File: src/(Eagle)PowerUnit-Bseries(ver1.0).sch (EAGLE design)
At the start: 142 parts, among them CON1 XT90PW-M, CON2 XT90PW-F, CON3 XT60PW-F, CON4 XT60PW-F, CON5 XT60PW-F, CON6 XT60PW-F, Q2 SSM3J332R, Q4 SSM3J332R, SW1 SS-12SDP2, SW2 RDS-16S-1055-SMT-TR, U1 LQFP64, U2 MCP2517FD, U3 CH340E, U5 AP63205WU-7, U7 AP331AWG-7, U9 AP331AWG-7, X1 XRCGB40M000F4M00R0, X2 RH100-24.000-18-1020-EXT-TR, X3 32.768K12.5PI/MC306

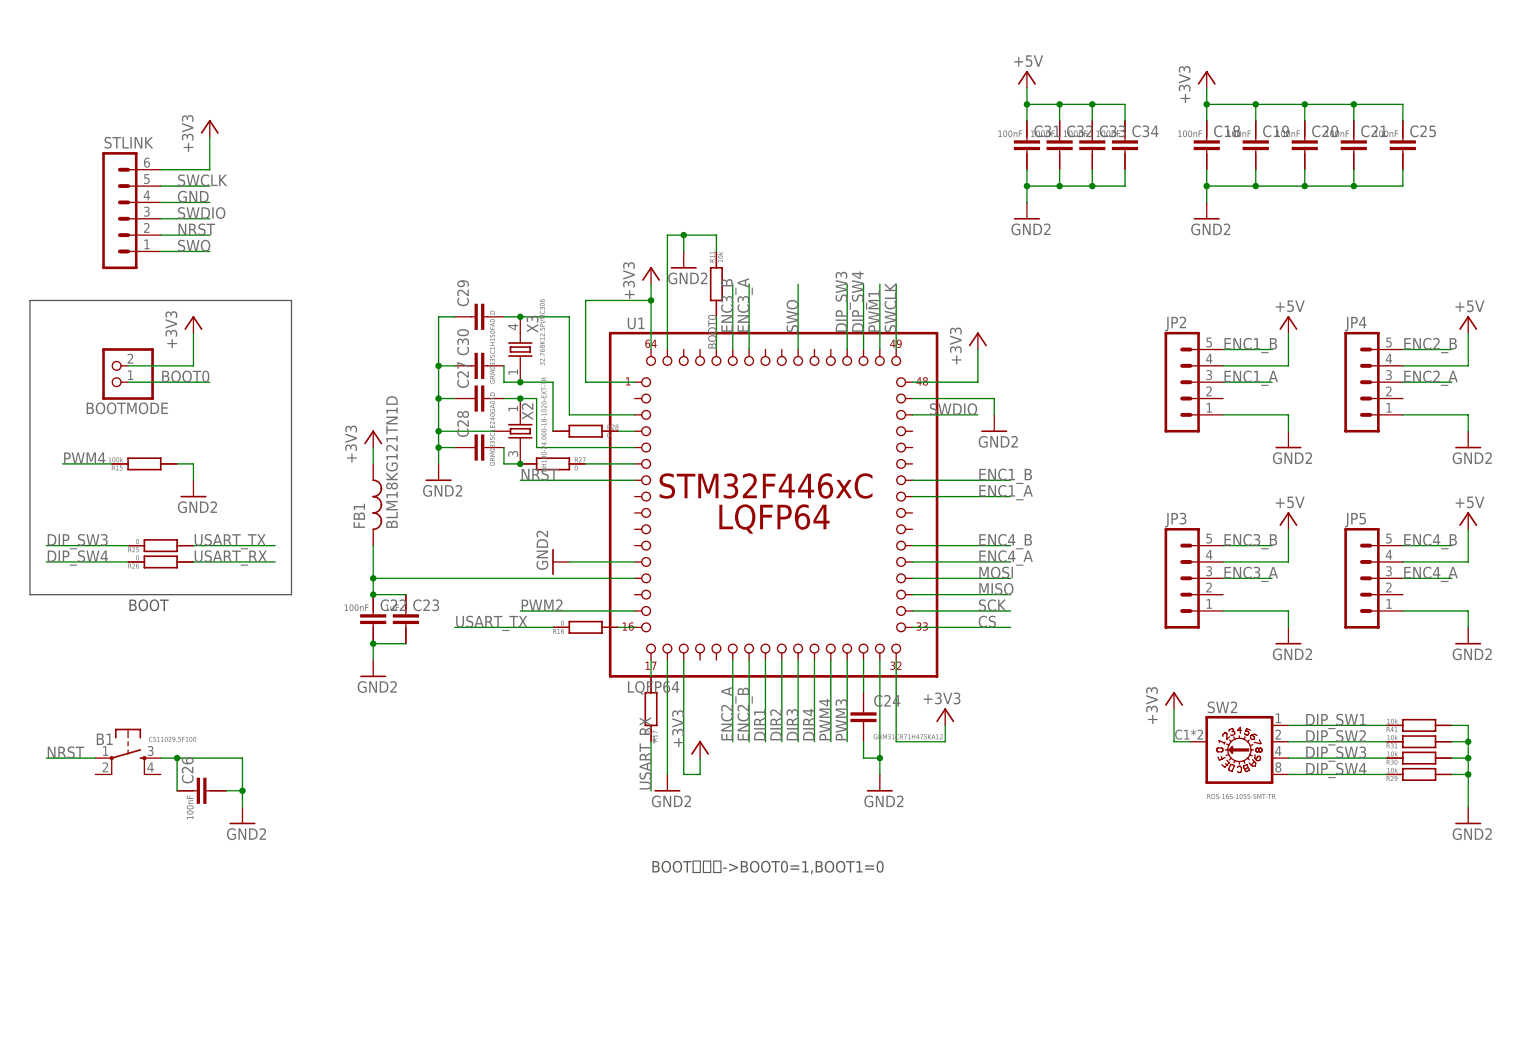
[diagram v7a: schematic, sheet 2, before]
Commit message: RJ45の追加
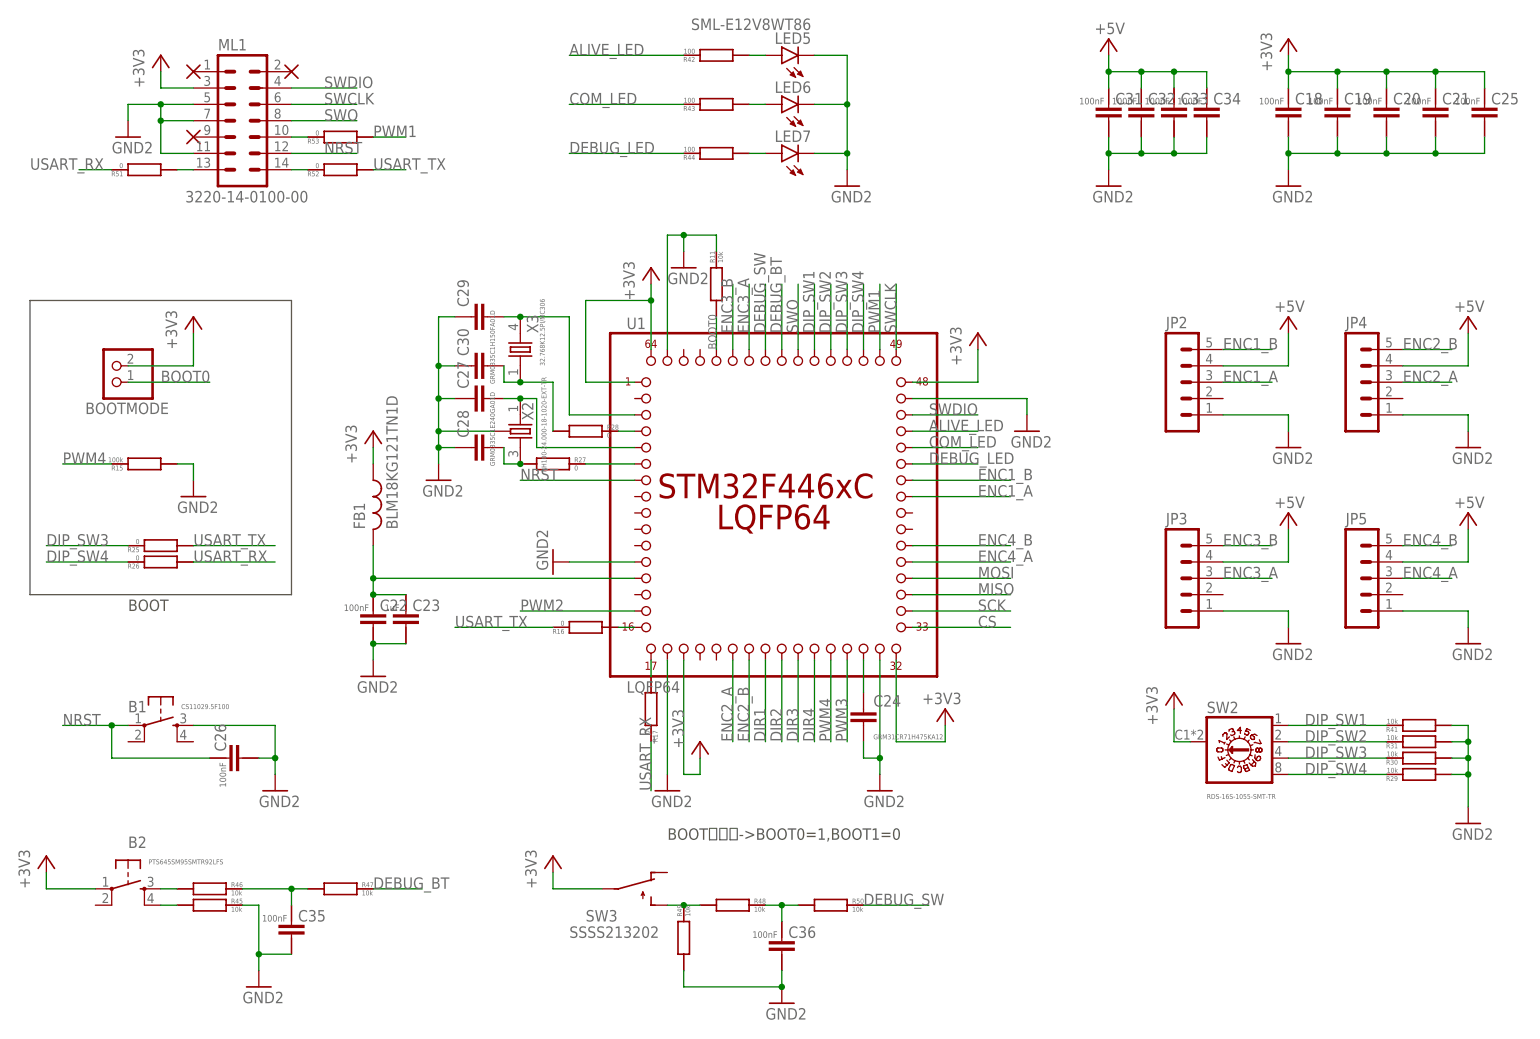
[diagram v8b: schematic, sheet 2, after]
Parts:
- removed STLINK: (no value), con-jst-xh:06-JST
- added B2: PTS645SM95SMTR92LFS, PTS645SM95SMTR92LFS:PTS645SM95SMTR92LFS
- added C35, C36: GCM188L81H104KA57, GCM188L81H104K57(0.1uF):GCM188L81H104KA57
- added LED5, LED6, LED7: SML-E12V8WT86, SML-E12V8WT86:SML-E12V8WT86
- added ML1: 3220-14-0100-00, 3220-14-0100-00:3220-14-0100-00
- added R42, R43, R44: 100, CR0603:CR0603
- added R45, R46, R47, R48, R49, R50: 10k, CR0603:CR0603
- added R51, R52, R53: 0, CR0603:CR0603
- added SW3: SSSS213202, SSSS213202:SSSS213202
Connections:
- new net ALIVE_LED: R42.RIGHT, U1.P45
- new net COM_LED: R43.RIGHT, U1.P44
- new net DEBUG_BT: C35.P$1, R46.RIGHT, R47.LEFT, R47.RIGHT, U1.P56
- new net DEBUG_LED: R44.RIGHT, U1.P43
- new net DEBUG_SW: R50.RIGHT, U1.P57
- new net N$58: LED5.A, R42.LEFT
- new net N$59: LED6.A, R43.LEFT
- new net N$60: LED7.A, R44.LEFT
- new net N$61: B2.4, R45.LEFT
- new net N$62: B2.3, R46.LEFT
- new net N$63: R48.LEFT, R49.RIGHT, SW3.R
- new net N$64: ML1.13, R51.LEFT
- new net N$65: C36.P$1, R48.RIGHT, R50.LEFT
- new net N$66: ML1.14, R52.RIGHT
- new net N$67: ML1.10, R53.RIGHT
- net +3V3: now also B2.1, ML1.3, SW3.C; no longer STLINK.6
- net DIP_SW1: now also U1.P54
- net DIP_SW2: now also U1.P53
- net GND: no longer STLINK.4
- net GND2: now also C35.P$2, C36.P$2, LED5.C, LED6.C, LED7.C, ML1.11, ML1.5, ML1.7, R45.RIGHT, R49.LEFT; no longer C26.P$1
- net NRST: now also C26.P$1, ML1.12; no longer STLINK.2
- net PWM1: now also R53.LEFT
- net SWCLK: now also ML1.6; no longer STLINK.5
- net SWDIO: now also ML1.4; no longer STLINK.3
- net SWO: now also ML1.8; no longer STLINK.1
- net USART_RX: now also R51.RIGHT
- net USART_TX: now also R52.LEFT
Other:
- moved on the sheet: B1, C18, C19, C20, C21, C25, C26, C31, C32, C33, C34
